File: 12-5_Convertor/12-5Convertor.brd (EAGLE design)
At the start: 45.3 x 52.1 mm, 19 parts, among them IC1 ACS764, U1 LM2678

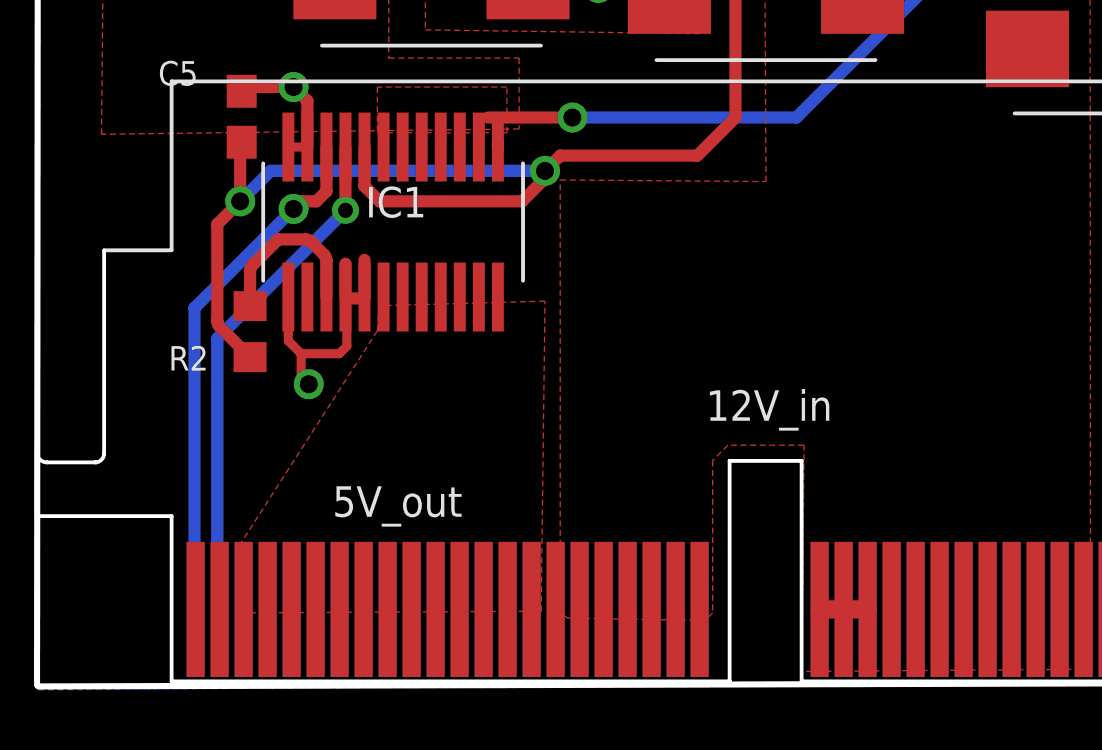
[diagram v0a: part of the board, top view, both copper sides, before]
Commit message: Changed the pin order of the backplane connector
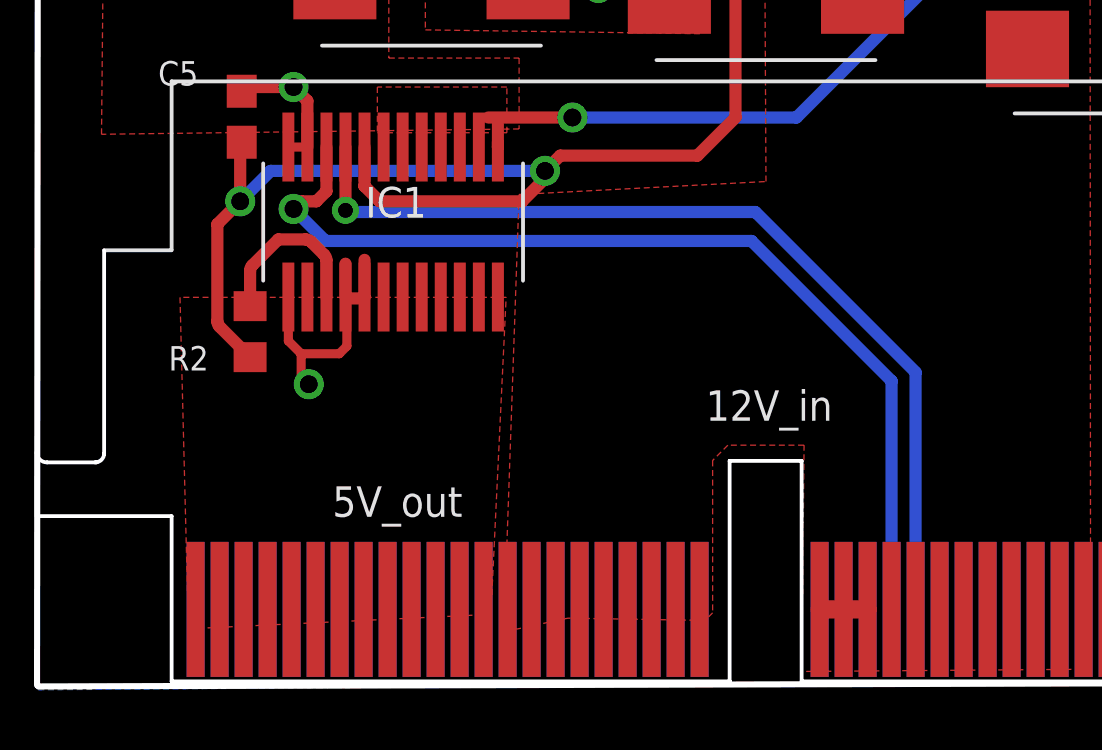
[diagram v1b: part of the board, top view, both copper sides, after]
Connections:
- net +12V: now also U$4.T14, U$4.T15; no longer U$4.T26
- net +5V: now also U$4.T1, U$4.T2
- net SCL: now also U$4.B26; no longer U$4.B1
- net SDA: now also U$4.B27; no longer U$4.B2
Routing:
- net SCL: track 17.5 -> 32.7 mm
- net SDA: track 17.2 -> 31.3 mm
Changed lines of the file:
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@@
 <?xml version="1.0" encoding="utf-8"?>
 <!DOCTYPE eagle SYSTEM "eagle.dtd">
-<eagle version="7.5.0">
+<eagle version="7.2.0">
 <drawing>
 <settings>
@@
 <wire x1="31.496" y1="22.6716" x2="32.039" y2="22.6716" width="0.4064" layer="1"/>
 <wire x1="32.039" y1="22.6716" x2="32.085" y2="22.7176" width="0.4064" layer="1"/>
-<wire x1="29.972" y1="20.828" x2="29.972" y2="20.066" width="0.3048" layer="1"/>
 <wire x1="29.972" y1="20.066" x2="30.226" y2="19.812" width="0.3048" layer="1"/>
+<wire x1="29.972" y1="20.066" x2="29.972" y2="20.828" width="0.3048" layer="1"/>
 </signal>
 <signal name="+12V">
@@
 <wire x1="47.1306" y1="38.354" x2="46.9786" y2="38.506" width="0.4064" layer="1"/>
 <contactref element="U$4" pad="T17"/>
-<contactref element="U$4" pad="T20"/>
 <contactref element="U$4" pad="T16"/>
 <contactref element="U$4" pad="T18"/>
-<contactref element="U$4" pad="T19"/>
 <contactref element="U$4" pad="T23"/>
 <contactref element="U$4" pad="T21"/>
-<contactref element="U$4" pad="T26"/>
 <contactref element="U$4" pad="T22"/>
 <contactref element="U$4" pad="T24"/>
 <contactref element="U$4" pad="T25"/>
-<polygon width="0.254" layer="1" thermals="no">
+<polygon width="0.254" layer="1" thermals="no" rank="2">
 <vertex x="46.228" y="37.846"/>
 <vertex x="47.498" y="38.1"/>
@@
 <vertex x="43.434" y="11.938"/>
 <vertex x="38.862" y="12.0142"/>
-<vertex x="38.608" y="12.192"/>
-<vertex x="38.608" y="26.6192"/>
+<vertex x="36.7284" y="11.557"/>
+<vertex x="37.2364" y="26.1366"/>
 <vertex x="45.466" y="26.5684"/>
 <vertex x="45.4152" y="36.3982"/>
@@
 <wire x1="48.514" y1="38.862" x2="47.3346" y2="38.862" width="0.254" layer="1"/>
 <wire x1="47.3346" y1="38.862" x2="46.9786" y2="38.506" width="0.254" layer="1"/>
+<contactref element="U$4" pad="T14"/>
+<contactref element="U$4" pad="T15"/>
+<contactref element="U$4" pad="T19"/>
+<contactref element="U$4" pad="T20"/>
 </signal>
 <signal name="+5V">
@@
 <contactref element="IC1" pad="24"/>
 <polygon width="0.254" layer="1" thermals="no">
-<vertex x="27.94" y="14.478"/>
-<vertex x="27.94" y="12.192"/>
-<vertex x="37.973" y="12.2428"/>
-<vertex x="38.1" y="22.5806"/>
-<vertex x="32.5628" y="22.4282"/>
-<vertex x="32.512" y="21.59"/>
+<vertex x="26.2128" y="11.6586"/>
+<vertex x="36.2966" y="12.1412"/>
+<vertex x="36.8046" y="22.7076"/>
+<vertex x="25.9334" y="22.7076"/>
 </polygon>
 <contactref element="U$4" pad="T6"/>
@@
 <contactref element="U$4" pad="T13"/>
 <contactref element="U$4" pad="T11"/>
+<contactref element="U$4" pad="T2"/>
+<contactref element="U$4" pad="T1"/>
 </signal>
 <signal name="+3V3">
@@
 </signal>
 <signal name="SDA">
-<contactref element="U$4" pad="B2"/>
 <contactref element="IC1" pad="9"/>
 <wire x1="31.45" y1="27.7176" x2="31.45" y2="25.608" width="0.4064" layer="1"/>
 <via x="31.45" y="25.608" extent="1-16" drill="0.5"/>
-<wire x1="31.45" y1="25.608" x2="27.178" y2="21.336" width="0.4064" layer="16"/>
-<wire x1="27.178" y1="21.336" x2="27.178" y2="12.382" width="0.4064" layer="16"/>
-<wire x1="27.178" y1="12.382" x2="27.254" y2="12.306" width="0.4064" layer="16"/>
+<contactref element="U$4" pad="B27"/>
+<wire x1="50.454" y1="12.306" x2="50.454" y2="20.2088" width="0.4064" layer="16"/>
+<wire x1="50.454" y1="20.2088" x2="45.1104" y2="25.5524" width="0.4064" layer="16"/>
+<wire x1="45.1104" y1="25.5524" x2="31.5056" y2="25.5524" width="0.4064" layer="16"/>
+<wire x1="31.5056" y1="25.5524" x2="31.45" y2="25.608" width="0.4064" layer="16"/>
 </signal>
 <signal name="N$8">
@@
 </signal>
 <signal name="SCL">
-<contactref element="U$4" pad="B1"/>
 <contactref element="IC1" pad="10"/>
 <wire x1="30.815" y1="27.7176" x2="30.815" y2="26.243" width="0.4064" layer="1"/>
@@
 <wire x1="29.972" y1="25.908" x2="29.718" y2="25.654" width="0.4064" layer="1"/>
 <via x="29.718" y="25.654" extent="1-16" drill="0.6"/>
-<wire x1="29.718" y1="25.654" x2="26.416" y2="22.352" width="0.4064" layer="16"/>
-<wire x1="26.416" y1="22.352" x2="26.416" y2="12.344" width="0.4064" layer="16"/>
-<wire x1="26.416" y1="12.344" x2="26.454" y2="12.306" width="0.4064" layer="16"/>
+<contactref element="U$4" pad="B26"/>
+<wire x1="49.654" y1="12.306" x2="49.654" y2="19.9166" width="0.4064" layer="16"/>
+<wire x1="49.654" y1="19.9166" x2="44.9834" y2="24.5872" width="0.4064" layer="16"/>
+<wire x1="44.9834" y1="24.5872" x2="30.7848" y2="24.5872" width="0.4064" layer="16"/>
+<wire x1="30.7848" y1="24.5872" x2="29.718" y2="25.654" width="0.4064" layer="16"/>
 </signal>
 </signals>

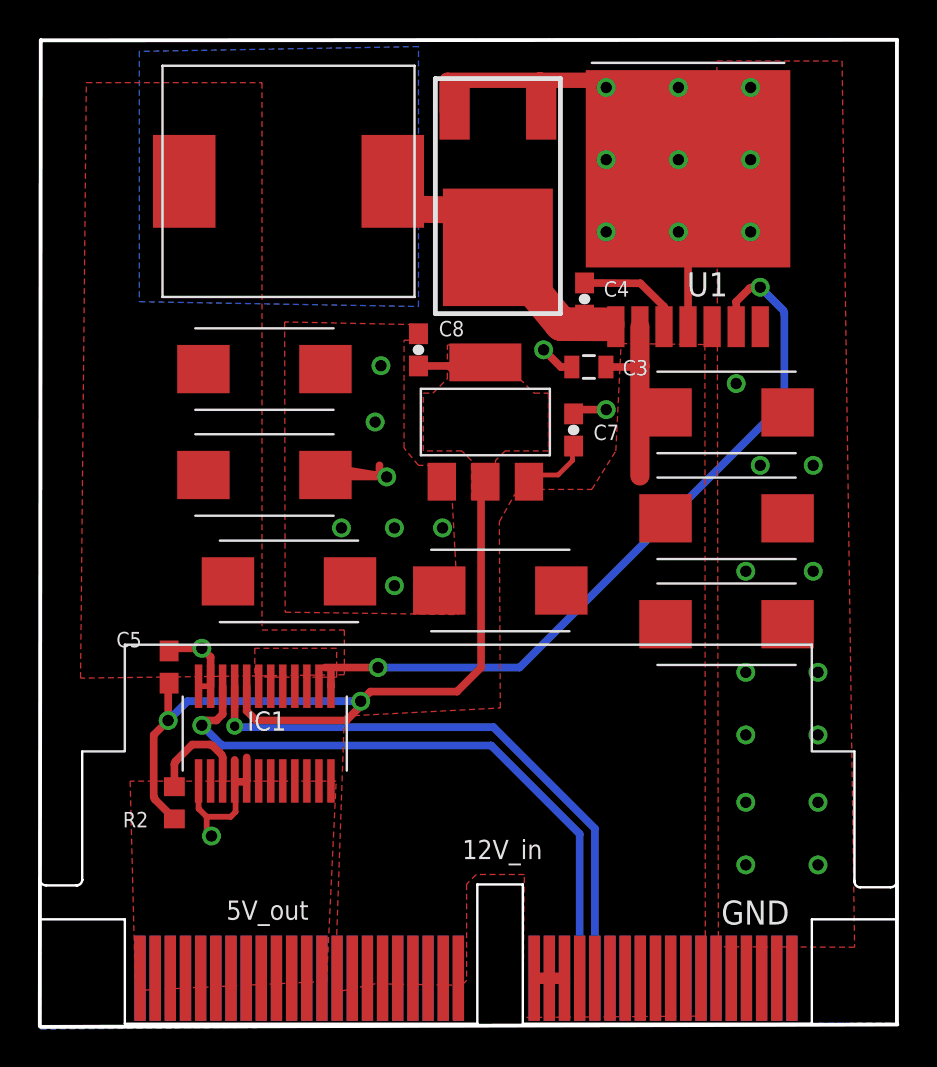
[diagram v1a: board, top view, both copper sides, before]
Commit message: Fixed errors on routing
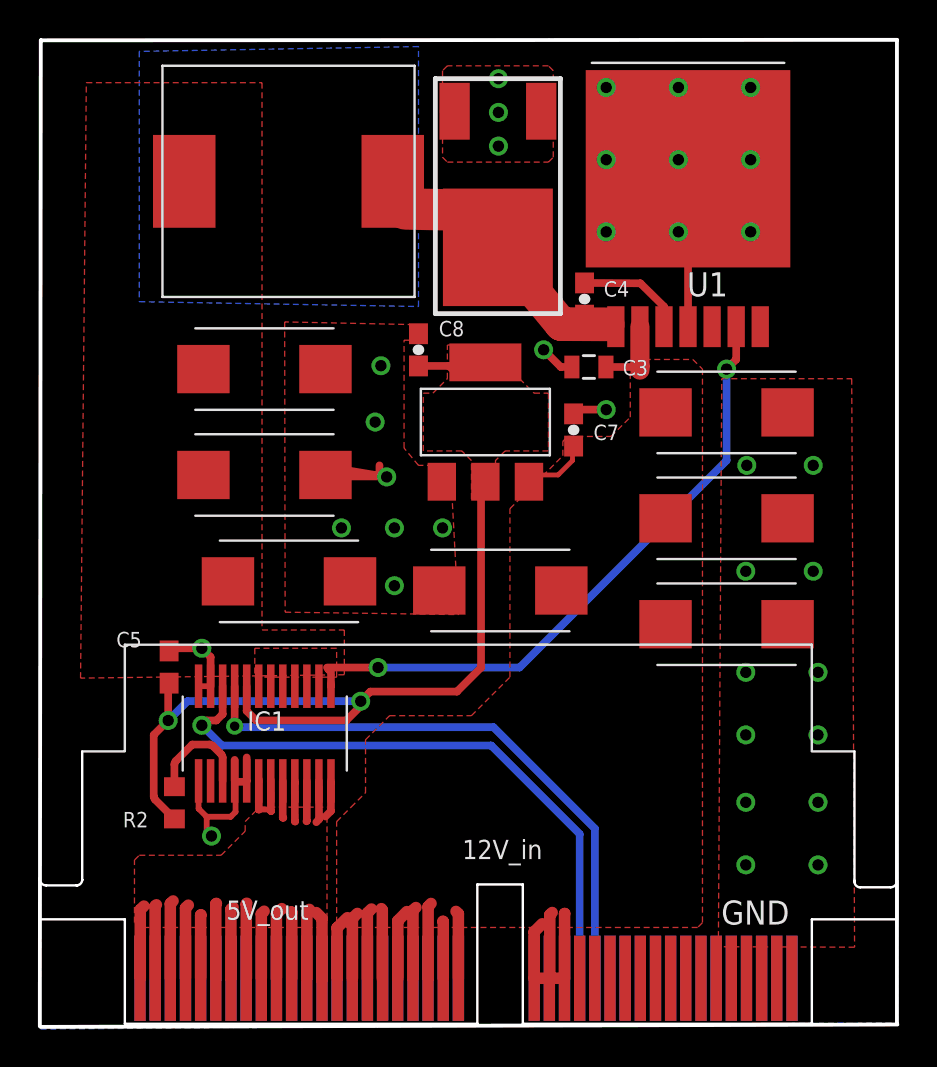
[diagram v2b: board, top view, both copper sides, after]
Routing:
- net +5V: track 0.00 -> 64.4 mm
- net +12V: track 15.0 -> 52.6 mm
- net GND: track 46.9 -> 33.5 mm, vias 33 -> 35
- net VOUT: track 39.7 -> 34.1 mm
